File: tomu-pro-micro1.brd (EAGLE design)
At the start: 32 x 18 mm, 19 parts, among them SW1 SPST_TACT-KMR2, U1 EFM32HG309F64G

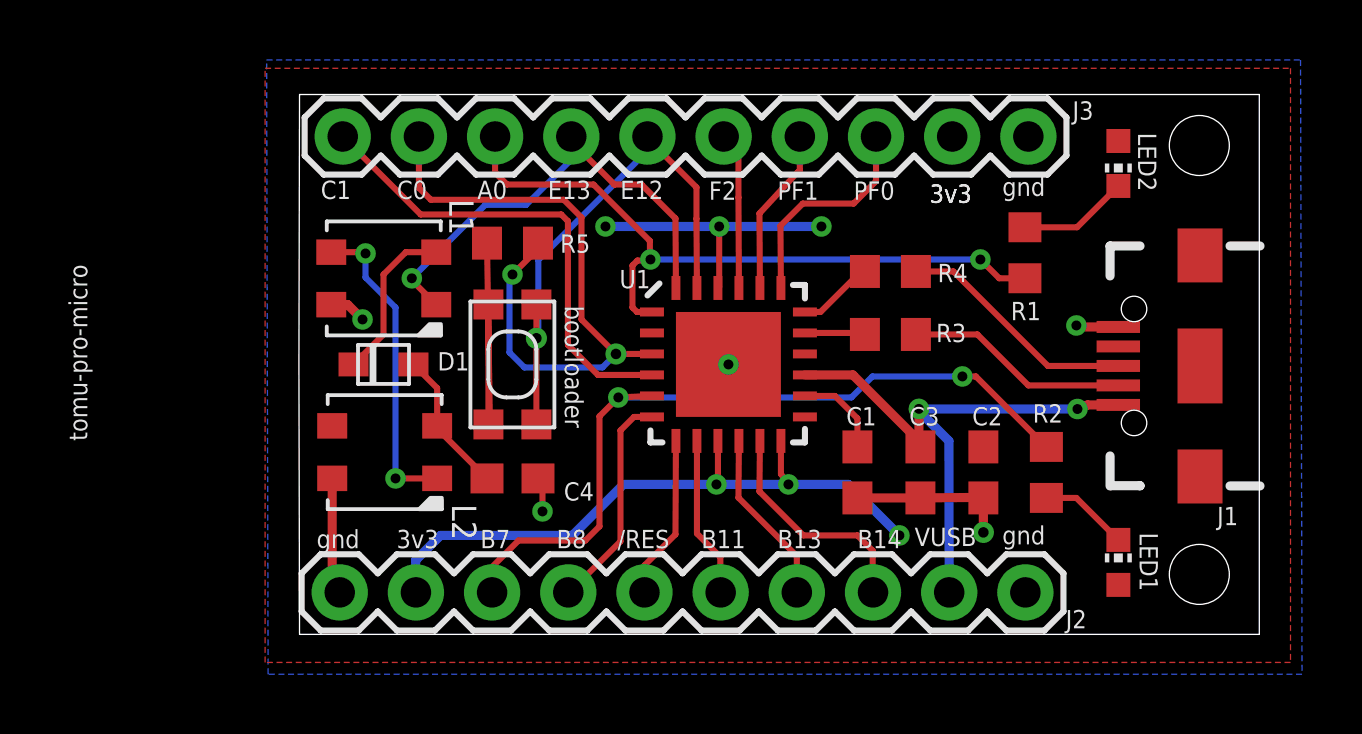
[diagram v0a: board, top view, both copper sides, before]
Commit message: fix EFM32HG309 QFN pad spacing issue. omg what a slog
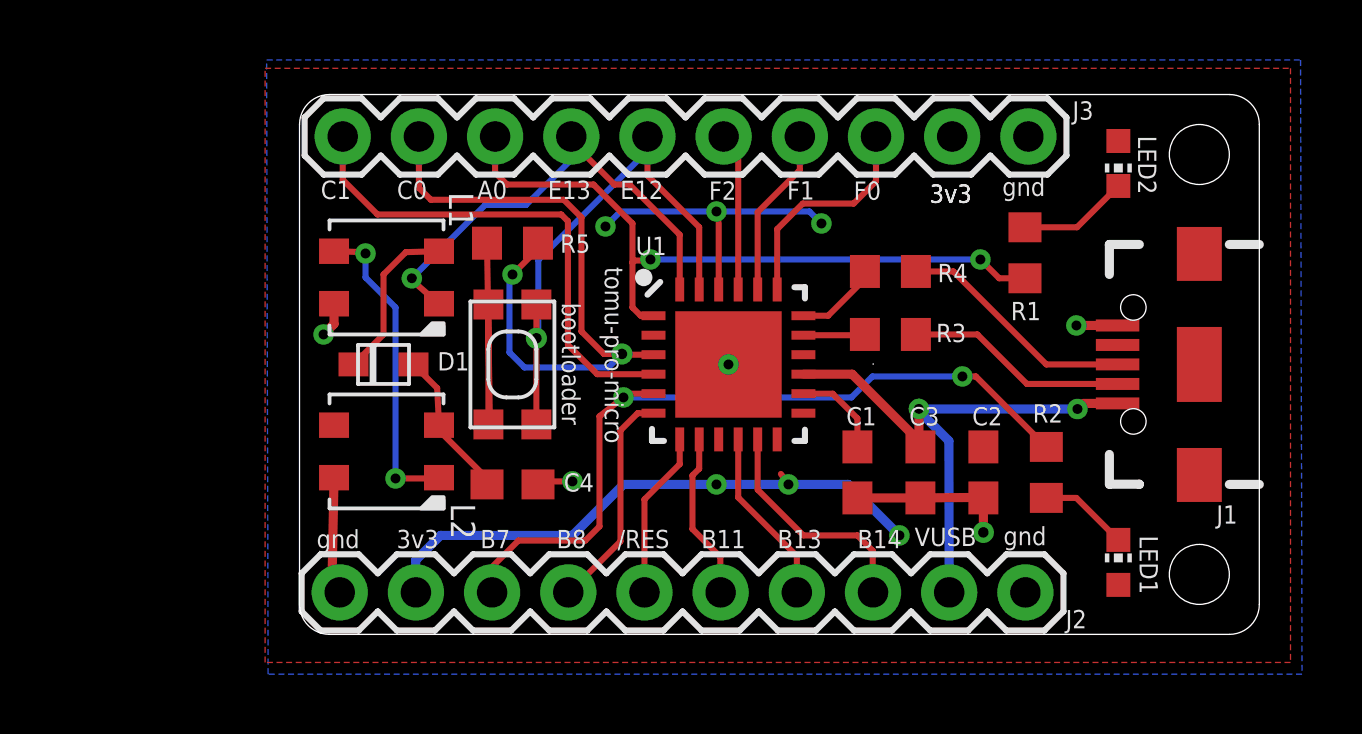
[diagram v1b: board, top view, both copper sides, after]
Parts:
- moved C4 0.20 mm to (-7.20, -4.00)
- moved L1 0.10 mm to (-11.4, 2.90)
- moved L2 0.07 mm to (-11.4, -2.90)
- moved J1 0.06 mm to (15.7, 0.00)
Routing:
- net +3V3: track 31.2 -> 29.3 mm
- net PC1: track 16.0 -> 16.9 mm
- net RUSB_P: track 2.53 -> 3.15 mm
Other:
- outline, holes or cut-outs redrawn
- board text added: "F0"
- board text added: "F1"
- board text added: "LED1"
- board text added: "LED2"
- board text added: "LEU0_RX"
- board text added: "LEU0_TX"
- board text added: "NEOLED_DIN"
- board text added: "SWDC"
- board text added: "SWDD"
- board text removed: "PF0"
- board text removed: "PF1"
